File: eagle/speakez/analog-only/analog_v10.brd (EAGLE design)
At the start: 34.5 x 43.2 mm, 51 parts, among them U1 +12v, U2 MAX5486

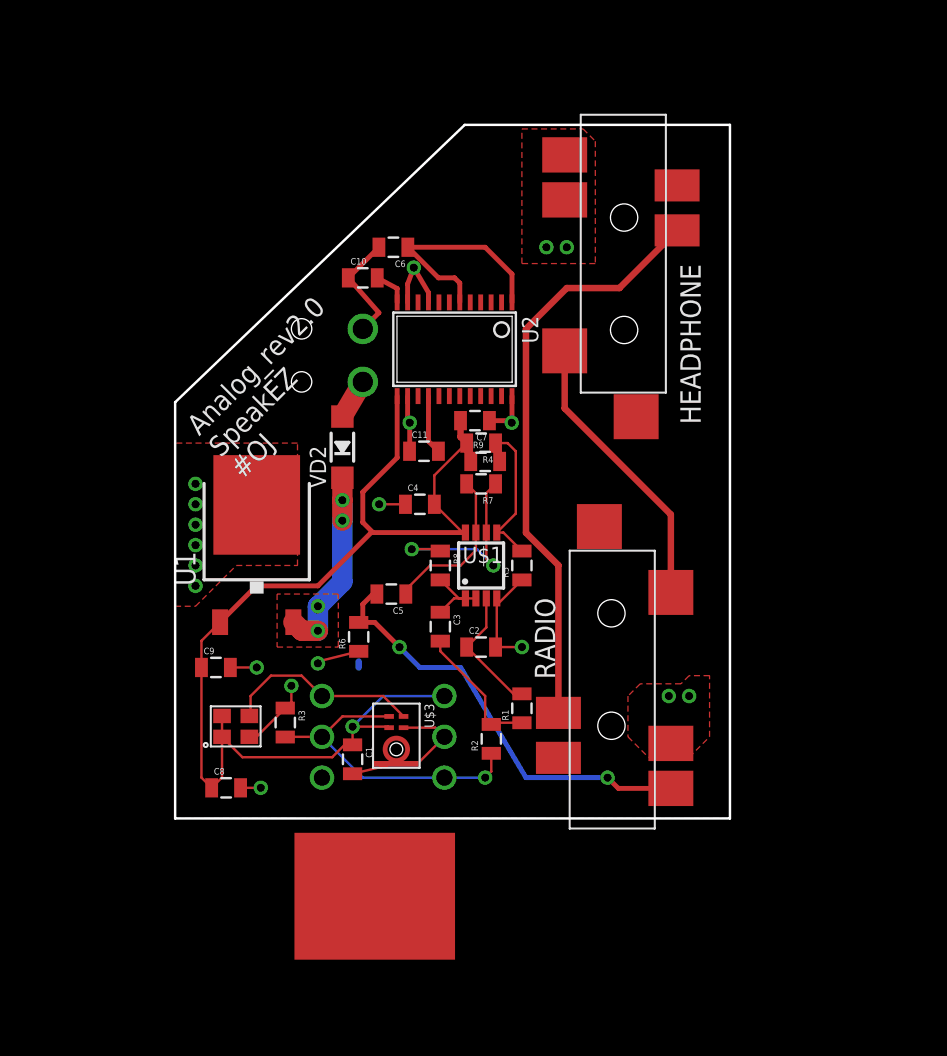
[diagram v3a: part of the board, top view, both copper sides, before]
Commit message: resized board
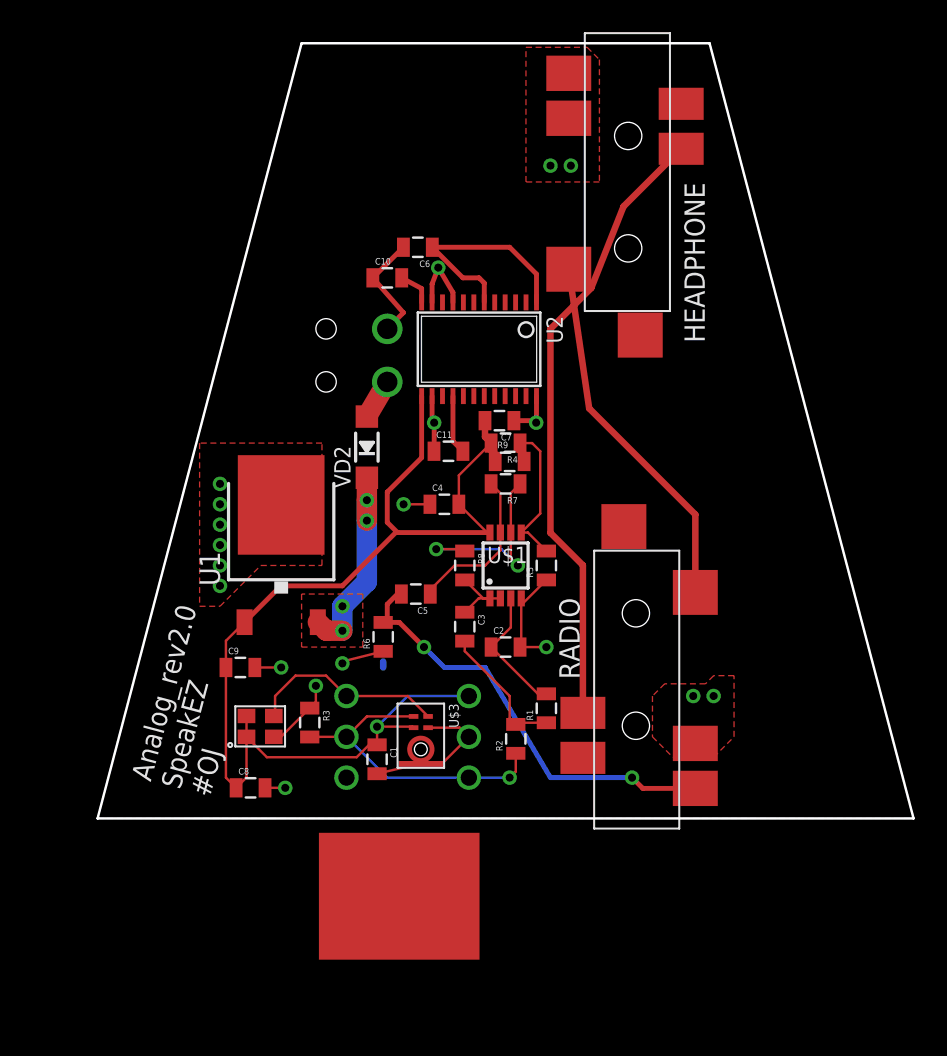
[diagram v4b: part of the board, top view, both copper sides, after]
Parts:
- moved HEADPHONE 5.09 mm to (28.2, 48.3)
- moved C2 1.52 mm to (22.9, 11.9)
- moved C3 1.52 mm to (20.3, 13.2)
- moved C4 1.52 mm to (19.1, 20.8)
- moved C6 1.52 mm to (17.4, 36.8)
- moved C7 1.52 mm to (22.5, 26.0)
- moved R2 1.52 mm to (23.5, 6.22)
- moved R4 1.52 mm to (22.9, 24.6)
- moved R6 1.52 mm to (15.2, 12.6)
- moved R7 1.52 mm to (22.9, 22.1)
- moved R8 1.52 mm to (20.3, 17.0)
- moved R9 1.52 mm to (23.1, 23.5)
- moved RADIO 1.52 mm to (33.3, 2.54)
- moved U$1 1.52 mm to (22.9, 17.0)
- moved U1 1.52 mm to (8.89, 18.3)
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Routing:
- net LEFT: track 17.8 -> 23.0 mm
- net RIGHT: track 36.7 -> 38.9 mm
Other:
- board size 34.5 x 43.2 mm -> 50.8 x 48.3 mm

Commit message: all components on, ugly ugly routing
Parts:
- removed HEADPHONE: SJ-43514-SMT, 35mm_audio:35MM_SMD_4WIRE
- added HP: SJ-43514-SMT, 35mm_audio:35MM_SMD_4WIRE
- moved R27 123.3 mm to (17.4, 42.4)
- moved R26 107.8 mm to (27.9, 20.3)
- moved R23 107.7 mm to (32.1, 28.4)
- moved R22 106.4 mm to (32.6, 17.5)
- moved R21 105.0 mm to (33.7, 24.0)
- moved C14 103.8 mm to (31.1, 19.9)
- moved C15 102.9 mm to (28.4, 22.7)
- moved R24 102.6 mm to (29.2, 26.4)
- moved R25 102.6 mm to (32.6, 26.2)
- moved R19 102.4 mm to (20.8, 44.3)
- moved R20 101.1 mm to (17.9, 45.8), turned to 180 degrees
- moved R17 99.0 mm to (31.1, 22.7), turned to 90 degrees
- moved C13 98.1 mm to (28.2, 30.5), turned to 90 degrees
- moved C12 94.3 mm to (24.0, 26.7)
- moved R18 94.3 mm to (25.3, 30.1), turned to 270 degrees
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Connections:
- net GND: now also HP.P$1, HP.P$4; no longer HEADPHONE.P$1, HEADPHONE.P$4
- net LEFT: now also HP.P$2; no longer HEADPHONE.P$2
- net RIGHT: now also HP.P$3, R27.2; no longer HEADPHONE.P$3
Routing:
- net VCC: track 84.9 -> 65.0 mm
- net GND: track 41.9 -> 33.1 mm
- net BIAS: track 8.33 -> 0.88 mm, vias 1 -> 0
- net RIGHT: track 38.9 -> 44.5 mm
- net AUDIO_AMPD: track 27.2 -> 32.5 mm
- net N$12: track 2.27 -> 0.00 mm
- net LEFT: track 23.0 -> 25.2 mm
- net VOUT_AMP: track 9.97 -> 12.2 mm

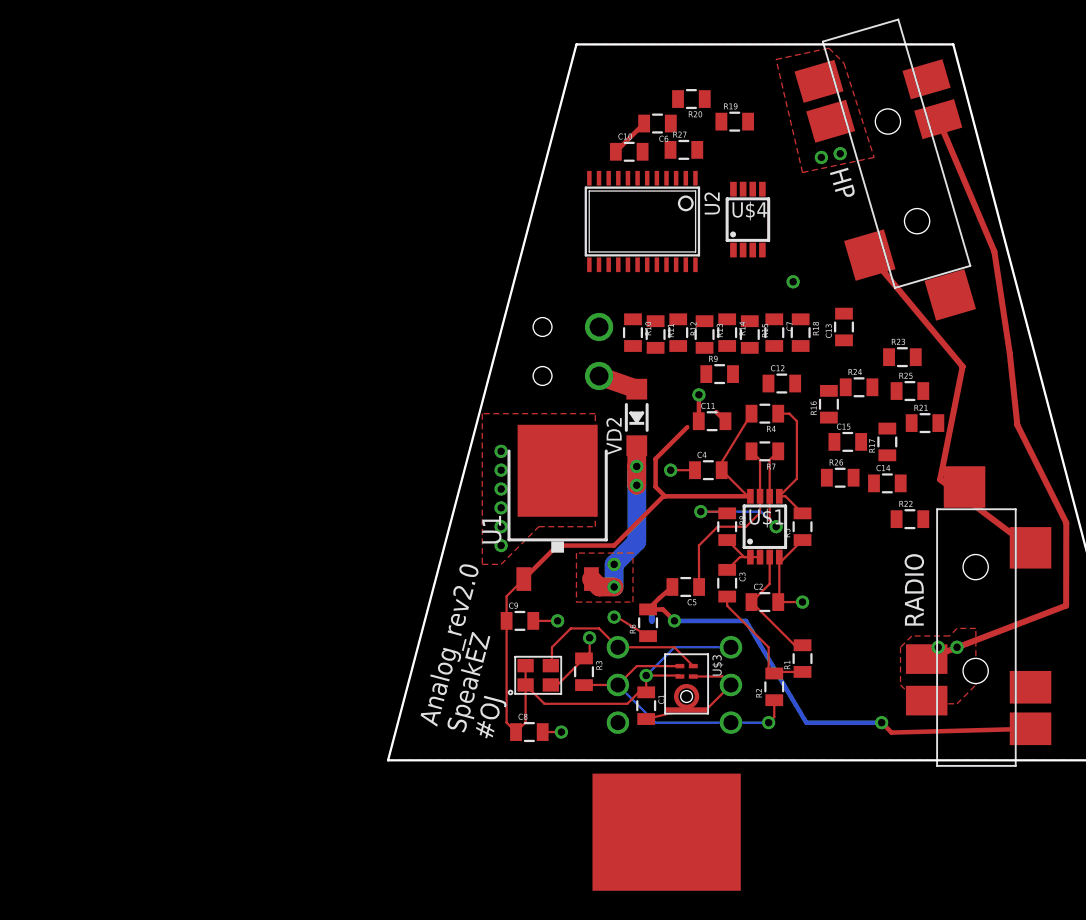
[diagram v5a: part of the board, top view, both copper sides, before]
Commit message: update L/R buffering, offsets, naming conventions, move info from nets layer to info layer
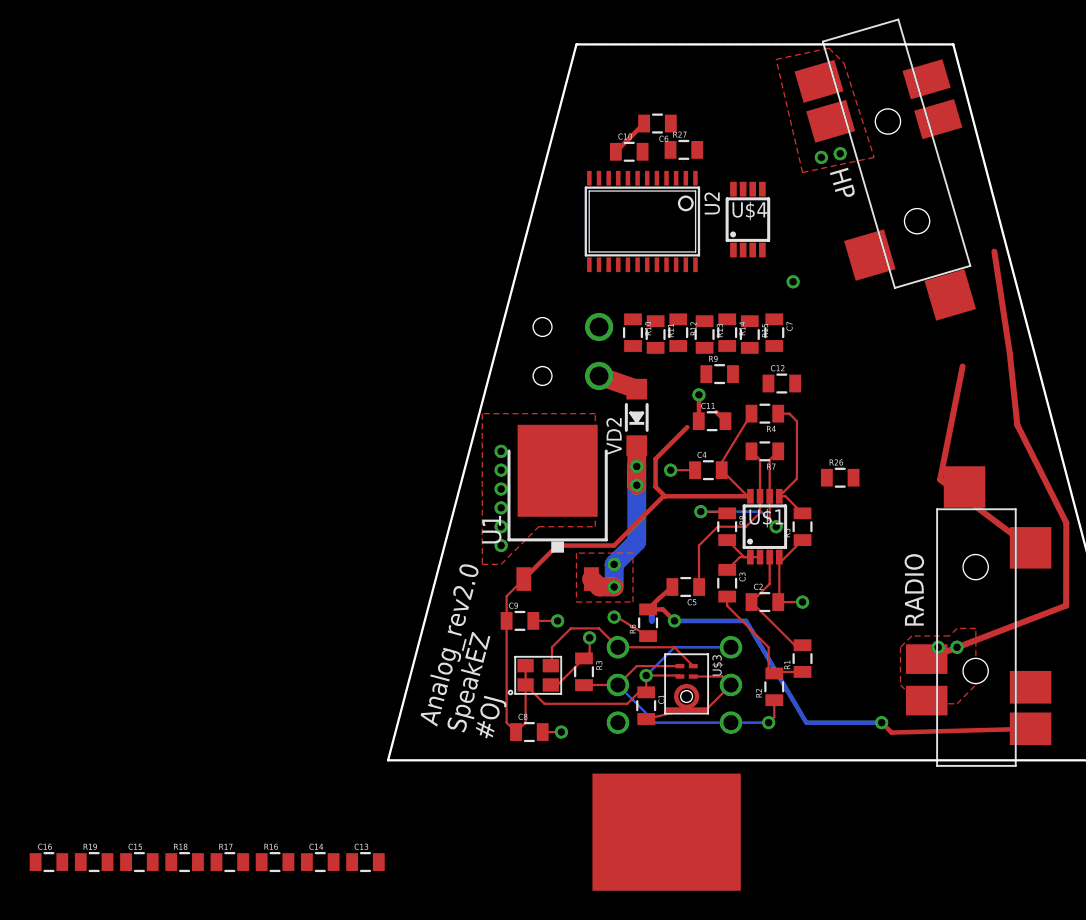
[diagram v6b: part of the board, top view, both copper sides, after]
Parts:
- removed R20, R24, R25: 1k, SparkFun-Resistors:0805
- removed R21, R22: 1k, SparkFun-Passives:0805
- removed R23: 100k, SparkFun-Resistors:0805
- added C16: 0.1 uF, SparkFun-Passives:0805
- R16, R17: value 1k -> 100k; device SparkFun-Passives:0805 -> SparkFun-Resistors:0805
- R19: value 1k -> 100k
- moved R19 66.0 mm to (-22.4, -5.59)
- moved C15 55.5 mm to (-19.3, -5.59)
- moved R18 54.8 mm to (-16.3, -5.59), turned to 0 degrees
- moved R17 52.6 mm to (-13.2, -5.59), turned to 0 degrees
- moved R16 48.4 mm to (-10.2, -5.59), turned to 0 degrees
- moved C13 48.4 mm to (-4.06, -5.59), turned to 0 degrees
- moved C14 46.0 mm to (-7.11, -5.59)
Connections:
- new net LEFT_OFFSET: C16.2, R19.2, U2.17
- new net RIGHT_OFFSET: C15.2, R18.2, U2.8
- net BIAS: now also R18.1, R19.1
- net GND: now also R16.1, U$4.4; no longer C14.1, R18.1, R22.1, R23.1
- net HEADPH_L: now also U$4.3; no longer R25.2
- net HEADPH_R: now also U$4.5; no longer R20.2
- net HP_L_AMPD: now also C14.1, HP.P$2, R17.2; no longer C15.2, R23.2
- net HP_R_AMPD: now also HP.P$3, R16.2; no longer R18.2
- net LEFT: now also C16.1; no longer HP.P$2, U2.17
- net N$10: now also C13.1, U$4.7; no longer R19.1, R20.1
- net N$14: now also C14.2, U$4.1, U$4.2; no longer R24.1, R25.1, U$4.3
- net RIGHT: now also C15.1; no longer HP.P$3, U2.8
- net VCC: no longer C14.2, R16.2, R21.2, U$4.1
- net VIRT_GND: no longer R16.1, R17.2, R21.1, R22.2, U$4.4, U$4.5
- net VOUT_AMP: no longer C13.1, C15.1, R19.2, R24.2, U$4.2, U$4.7
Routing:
- net LEFT: track 25.2 -> 15.4 mm
- net RIGHT: track 44.5 -> 34.8 mm

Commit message: routed some of board
but doubting my routing
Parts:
- moved C15 62.0 mm to (18.3, 43.7), turned to 270 degrees
- moved R16 54.8 mm to (13.2, 43.9)
- moved C13 54.6 mm to (15.2, 45.5), turned to 180 degrees
- moved R17 52.0 mm to (21.1, 33.5), turned to 270 degrees
- moved R19 47.1 mm to (7.37, 31.0), turned to 270 degrees
- moved C14 46.6 mm to (18.3, 33.5), turned to 90 degrees
- moved R18 46.5 mm to (8.13, 34.0), turned to 90 degrees
- moved C16 45.8 mm to (6.35, 27.4), turned to 90 degrees
- moved VD2 14.7 mm to (29.0, 23.9), turned to 270 degrees
- moved R26 14.5 mm to (14.0, 24.1), turned to 180 degrees
- moved R10 6.19 mm to (8.38, 27.4)
- moved C10 6.15 mm to (9.91, 47.1), turned to 180 degrees
- moved R11 5.68 mm to (10.4, 27.4)
- moved R12 5.01 mm to (12.7, 27.6)
- moved R27 4.75 mm to (16.1, 47.0)
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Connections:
- net GND renamed HEADPHONES_R
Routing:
- net RIGHT: track 34.8 -> 0.00 mm
- net HP_R_AMPD: track 0.00 -> 26.9 mm
- net VBATSAFE: track 13.2 -> 29.3 mm
- net VCC: track 65.0 -> 80.0 mm
- net LEFT: track 15.4 -> 5.13 mm
- net LEFT_OFFSET: track 0.00 -> 9.17 mm
- net N$11: track 0.00 -> 9.00 mm
- net RIGHT_OFFSET: track 0.00 -> 8.51 mm, vias 0 -> 1
- net N$13: track 0.00 -> 7.94 mm
- net N$5: track 0.00 -> 7.54 mm
- net BIAS: track 0.88 -> 8.29 mm
- net N$12: track 0.00 -> 7.22 mm
- net N$6: track 0.00 -> 6.97 mm
- net N$8: track 0.00 -> 6.16 mm
- net N$9: track 0.00 -> 6.16 mm
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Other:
- board size 50.8 x 48.3 mm -> 49.5 x 48.3 mm

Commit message: did some more layout, fixed some random things
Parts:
- moved R18 49.9 mm to (57.7, 27.7)
- moved R17 33.4 mm to (54.1, 28.4)
- moved C14 31.4 mm to (48.8, 25.9)
- moved VD2 30.0 mm to (2.54, 9.65)
- moved R27 27.1 mm to (26.7, 22.0), turned to 270 degrees
- moved C12 25.4 mm to (49.0, 29.0)
- moved C11 16.0 mm to (8.89, 36.3)
- moved C10 14.1 mm to (18.8, 36.2), turned to 0 degrees
- moved R26 13.1 mm to (25.4, 17.8), turned to 0 degrees
- moved R15 12.9 mm to (8.89, 26.7), turned to 180 degrees
- moved C7 12.3 mm to (14.7, 36.2), turned to 180 degrees
- moved C16 11.8 mm to (17.8, 24.6), turned to 270 degrees
- moved R19 10.9 mm to (16.3, 24.6)
- moved R9 10.8 mm to (6.48, 27.2), turned to 270 degrees
- moved R14 10.7 mm to (8.89, 28.2), turned to 180 degrees
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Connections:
- net HEADPHONES_R renamed GND
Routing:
- net HP_R_AMPD: track 26.9 -> 1.62 mm
- net VBATSAFE: track 29.3 -> 10.5 mm, vias 4 -> 3
- net VCC: track 80.0 -> 91.6 mm, vias 2 -> 5
- net RIGHT_OFFSET: track 8.51 -> 0.00 mm, vias 1 -> 0
- net BIAS: track 8.29 -> 15.0 mm
- net LEFT: track 5.13 -> 0.00 mm
- net N$12: track 7.22 -> 2.27 mm
- net VIRT_GND: track 9.06 -> 4.31 mm
- net N$11: track 9.00 -> 4.37 mm
- net AUDIO_AMPD: track 28.7 -> 25.7 mm
- net N$2: track 8.18 -> 10.8 mm
- net AUDIO: track 4.61 -> 6.54 mm
- net N$13: track 7.94 -> 9.75 mm
- net N$9: track 6.16 -> 4.47 mm
- net VOUT_AMP: track 12.2 -> 13.8 mm
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- removed copper zone on layer 1, net VBATSAFE
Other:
- board size 49.5 x 48.3 mm -> 46.2 x 48.3 mm
